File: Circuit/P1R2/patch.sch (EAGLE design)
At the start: 34 parts, among them U1 MK20DX256VLH7, U2 TPS61200, Y1 32.768KHz, Y2 16Mhz/8pF

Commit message: Forum boards done
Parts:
- removed JP1: (no value), SparkFun-Connectors:M07
- removed LED: AMBER/ 592 nm, appfruits:LED-AMBER
- removed R30: 470, appfruits:RESISTOR-470
- added C10: 4.7 pF, SparkFun-Capacitors:CAP0603-CAP
- added C12: 1.0 pF, SparkFun-Capacitors:CAP0603-CAP
- added C13: 1.5 pF, SparkFun-Capacitors:CAP0603-CAP
- added C14, C15: 22 pF, SparkFun-Capacitors:CAP0603-CAP
- added C22: 1 uF, SparkFun-Capacitors:CAP0603-CAP
- added C23, C7: 15 pF, SparkFun-Capacitors:CAP0603-CAP
- added C24, C25: .1 uF, SparkFun-Capacitors:CAP0603-CAP
- added C6: 5.6 pF, SparkFun-Capacitors:CAP0603-CAP
- added C8: 33 nF, SparkFun-Capacitors:CAP0603-CAP
- added C9: 2.2 nF, SparkFun-Capacitors:CAP0603-CAP
- added JP5: (no value), SparkFun-Connectors:M02PTH
- added JP6: M100.1, umich:M100.1
- added L2: 2.7 nH, SparkFun-Passives:INDUCTOR0402
- added L5: 8.2 nH, SparkFun-Passives:INDUCTOR0402
- added L6: 3.9 nH, SparkFun-Passives:INDUCTOR0402
- added MESH: NRF24L01, RF:NRF24L01
- added R1, R5, R8: 12k, SparkFun-Resistors:RESISTOR0603-RES
- added R11: 1M, SparkFun-Resistors:RESISTOR0603-RES
- added R12: 22k, SparkFun-Resistors:RESISTOR0603-RES
- added R13, R14, R15: 10k, SparkFun-Resistors:RESISTOR0603-RES
- added S1: (no value), SparkFun-Electromechanical:SWITCH-SPDT-SMD-A
- added U$1, U$2: ANTENNA2SMD, SparkFun-RF:ANTENNA2SMD
- added U$3: 25Q40, wifi:25Q40
- added U3: MPU-9250, chips:MPU-9250
- added WIFI: ESP8266EX, wifi:ESP8266EX
- added Y3, Y4: 16 Mhz, SparkFun-FreqCtrl:CRYSTAL5X3
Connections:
- net 18/SDA renamed PTB3
- net 19/SCL renamed PTB2
- removed net 16: JP2.3, U1.PTB0
- removed net 17: JP2.4, U1.PTB1
- removed net 20: JP2.5
- removed net 28: LED.A, U1.PTC8
- removed net PGND: C1.2, C3.2, C4.2, U2.GND, U2.PAD@1, U2.PAD@2, U2.PAD@3, U2.PAD@4, U2.PAD@5, U2.PGND
- new net 3.3V1: C22.2, C24.2, C25.1, MESH.VDD/15, MESH.VDD/18, MESH.VDD/7, R8.2, U$3.VCC, U3.VDD, U3.VDDIO, WIFI.CHIP_EN/7, WIFI.VDD3P3/3, WIFI.VDD3P3/4, WIFI.VDDA/1, WIFI.VDDD/29, WIFI.VDDPST/11, WIFI.VDDPST/17
- new net CE: MESH.CE/1
- new net CSN: MESH.CSN/2
- new net GND1: C10.2, C12.2, C14.2, C15.2, C22.1, C23.2, C24.1, C25.2, C7.2, C8.1, C9.2, MESH.VSS/14, MESH.VSS/17, MESH.VSS/20, MESH.VSS/8, R12.2, R5.1, U$3.GND, WIFI.GND/33
- new net IQR: MESH.IRQ/6
- new net MISO: MESH.MISO/5
- new net MOSI: MESH.MOSI/4
- new net N$13: C6.2, WIFI.LNA/2
- new net N$16: C6.1, U$1.SIGNAL
- new net N$17: C14.1, MESH.XC2/9, R11.1, Y4.1
- new net N$19: C10.1, C9.1, L2.2, MESH.VDD_PA/11
- new net N$20: L5.1, L6.1, MESH.ANT2/13
- new net N$21: C8.2, MESH.DVDD/19
- new net N$22: MESH.GND
- new net N$23: L2.1, L5.2, MESH.ANT1/12
- new net N$24: MESH.IREF/16, R12.1
- new net N$25: C13.1, L6.2
- new net N$26: C12.1, C13.2, U$2.SIGNAL
- new net N$31: R8.1, WIFI.GPIO2/14
- new net N$32: R5.2, WIFI.MTCK/12
- new net N$33: U3.FSYNC
- new net N$34: U3.REGOUT
- new net N$35: U3.AUX_DA
- new net N$36: U3.AUX_CL
- new net N$37: U3.GND
- new net N$38: WIFI.RES12K/31
- new net N$39: U3.INT
- new net N$40: U3.!CS
- new net PTB0: U1.PTB0
- new net PTB1: U1.PTB1
- new net RST: R1.1, WIFI.EXT_RSTB/32
- new net RTC: WIFI.VDD_RTC/5
- new net RX_W: WIFI.U0TXD/26
- new net SCK: MESH.SCK/3
- new net SCL: R14.2
- new net SD-CLK: U$3.CLK, WIFI.SD_CLK/21
- new net SD-CMD: U$3.CS#, WIFI.SD_CMD/20
- new net SD-D0: U$3.DO, WIFI.SD_DATA_0/22
- new net SD-D1: U$3.DIO, WIFI.SD_DATA_1/23
- new net SD-D2: U$3.HOLD#, WIFI.SD_DATA_2/18
- new net SD-D3: U$3.WP#, WIFI.SD_DATA_3/19
- new net SDA: R13.2
- new net SDO: R15.2
- new net TOUT: WIFI.TOUT/6
- new net TX_W: WIFI.U0RXD/25
- new net VDD: R13.1, R14.1, R15.1, WIFI.VDDA/30
- new net VRAW: JP5.2, S1.P
- new net XTAL_IN: C23.1, WIFI.XTAL_IN/28, Y3.2
- new net XTAL_OUT: C7.1, WIFI.XTAL_OUT/27, Y3.1
- net 14: no longer JP2.1
- net 15: no longer JP2.2
- net 21: no longer JP2.6
- net 22: no longer JP2.7
- net 23: no longer JP2.8
- net 3.3V: now also JP6.1, LED1.A; no longer LED1.C
- net GND: now also C1.2, C3.2, C4.2, JP5.1, JP6.10, U2.GND, U2.PAD@1, U2.PAD@2, U2.PAD@3, U2.PAD@4, U2.PAD@5, U2.PGND; no longer R30.1
- net ID: now also JP6.6; no longer JP1.5
- net N$1: now also LED1.C; no longer LED1.A
- net N$18: now also C15.1, MESH.XC1/10, R11.2, Y4.2; no longer LED.C, R30.2
- net PTA2: now also JP6.3; no longer JP1.2
- net RESET_B: now also JP6.2; no longer JP1.1
- net SWD_CLK: now also JP6.4; no longer JP1.3
- net SWD_DIO: now also JP6.5; no longer JP1.4
- net USB_D_N: now also JP6.8; no longer JP1.7
- net USB_D_P: now also JP6.7; no longer JP1.6
- net VCC: now also JP6.9, S1.O

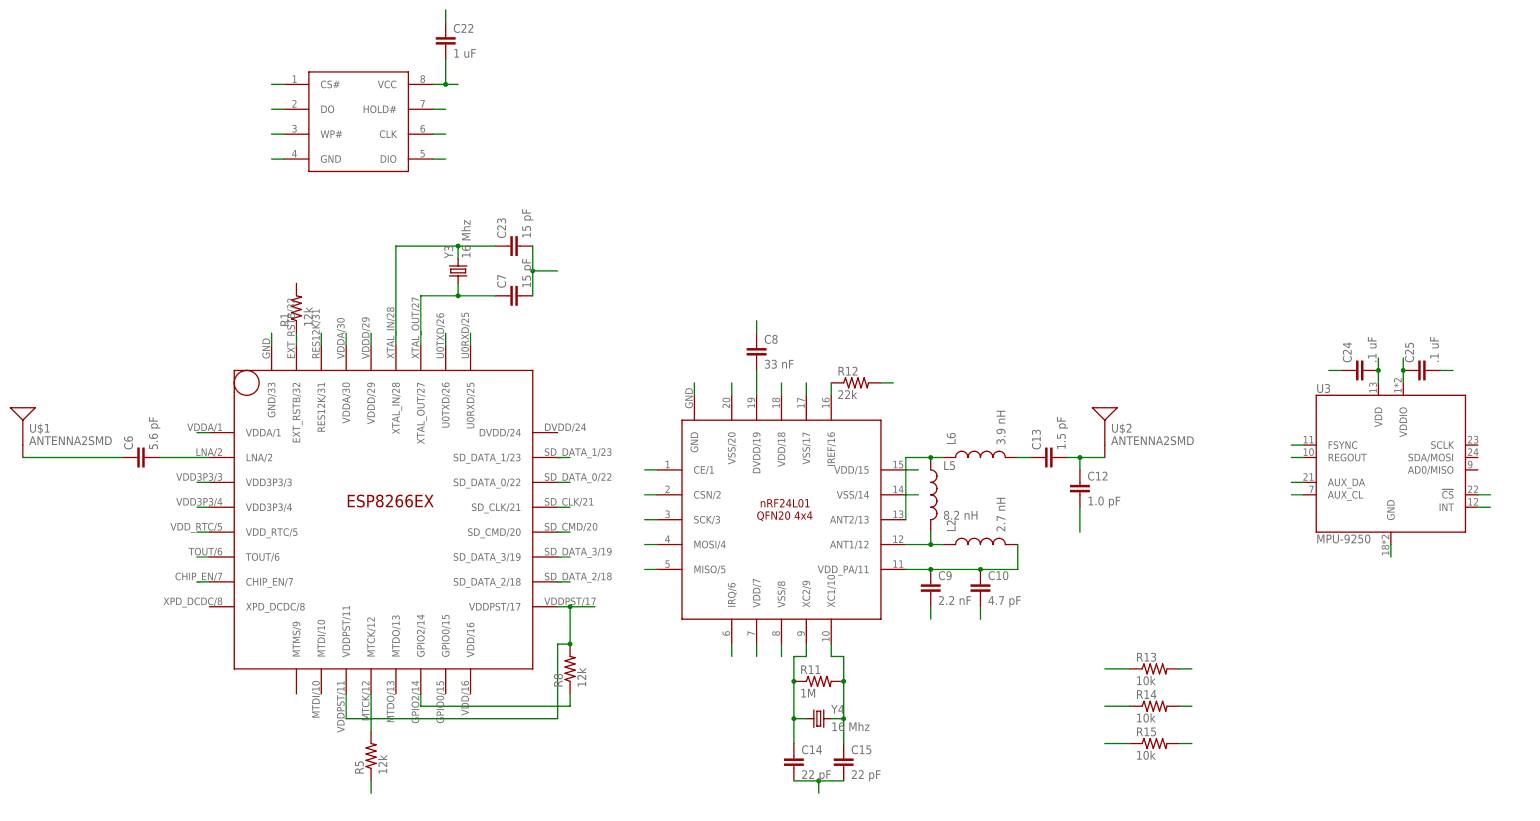
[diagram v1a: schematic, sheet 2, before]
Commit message: Mesh and IMU in place
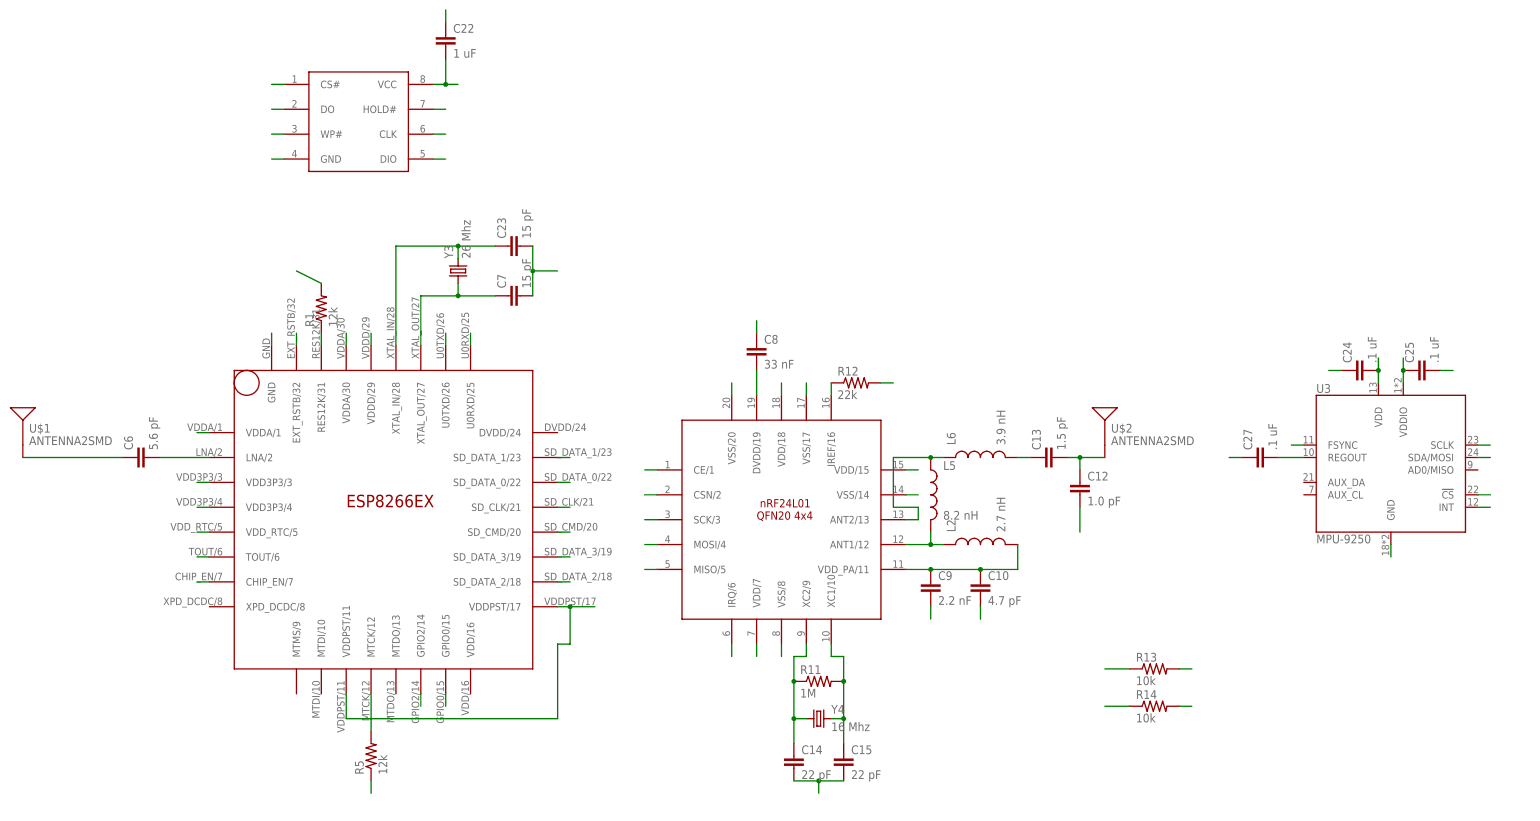
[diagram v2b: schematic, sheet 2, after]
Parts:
- removed R15: 10k, SparkFun-Resistors:RESISTOR0603-RES
- removed R8: 12k, SparkFun-Resistors:RESISTOR0603-RES
- added C27: .1 uF, SparkFun-Capacitors:CAP0603-CAP
- Y3: value 16 Mhz -> 26 Mhz
- renumbered MESH to U$4, WIFI to U$6
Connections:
- net 14 renamed PTD1
- net 2 renamed PTD0
- net 21 renamed PTD6
- net 23 renamed PTC2
- net 24 renamed PTA5
- net 26 renamed PTE1
- net 29 renamed PTC10
- net 3 renamed PTA12
- net 30 renamed PTC11
- net 31 renamed PTE0
- net 33 renamed PTA4
- net 4 renamed PTA13
- net 5 renamed PTD7
- net 6 renamed PTD4
- net 7 renamed PTD2
- net 8 renamed PTD3
- net 9 renamed PTC3
- net N$7 renamed PTD5
- removed net 0: U1.PTB16
- removed net 1: U1.PTB17
- removed net 10: U1.PTC4
- removed net 11/MOSI: U1.PTC6
- removed net 12/MISO: U1.PTC7
- removed net 13/SCK: U1.PTC5
- removed net 15: U1.PTC0
- removed net 22: U1.PTC1
- removed net 25: U1.PTB19
- removed net 27: U1.PTC9
- removed net 3.3V1: C22.2, C24.2, C25.1, R8.2, U$3.VCC, U$4.VDD/15, U$4.VDD/18, U$4.VDD/7, U$6.CHIP_EN/7, U$6.VDD3P3/3, U$6.VDD3P3/4, U$6.VDDA/1, U$6.VDDD/29, U$6.VDDPST/11, U$6.VDDPST/17, U3.VDD, U3.VDDIO
- removed net 32: U1.PTB18
- removed net CE: U$4.CE/1
- removed net CSN: U$4.CSN/2
- removed net GND1: C10.2, C12.2, C14.2, C15.2, C22.1, C23.2, C24.1, C25.2, C7.2, C8.1, C9.2, R12.2, R5.1, U$3.GND, U$4.VSS/14, U$4.VSS/17, U$4.VSS/20, U$4.VSS/8, U$6.GND/33
- removed net IQR: U$4.IRQ/6
- removed net MISO: U$4.MISO/5
- removed net MOSI: U$4.MOSI/4
- removed net N$22: U$4.GND
- removed net N$31: R8.1, U$6.GPIO2/14
- removed net N$33: U3.FSYNC
- removed net N$35: U3.AUX_DA
- removed net N$36: U3.AUX_CL
- removed net N$37: U3.GND
- removed net N$39: U3.INT
- removed net N$40: U3.!CS
- removed net RST: R1.1, U$6.EXT_RSTB/32
- removed net RX_W: U$6.U0TXD/26
- removed net SCK: U$4.SCK/3
- removed net SDO: R15.2
- removed net TX_W: U$6.U0RXD/25
- new net PTB16: U$6.U0RXD/25, U1.PTB16
- new net PTB17: U$6.U0TXD/26, U1.PTB17
- new net PTB18: U$6.GPIO0/15, U1.PTB18
- new net PTB19: U$6.GPIO2/14, U1.PTB19
- new net PTC0: U$6.EXT_RSTB/32, U1.PTC0
- new net PTC1: U$6.CHIP_EN/7, U1.PTC1
- new net PTC4: U$4.CSN/2, U1.PTC4
- new net PTC5: U$4.SCK/3, U1.PTC5
- new net PTC6: U$4.MOSI/4, U1.PTC6
- new net PTC7: U$4.MISO/5, U1.PTC7
- new net PTC8: U$4.IRQ/6, U1.PTC8
- new net PTC9: U$4.CE/1, U1.PTC9
- net 3.3V: now also C22.2, C24.2, C25.1, R13.1, R14.1, U$3.VCC, U$4.VDD/18, U$4.VDD/7, U$6.VDD3P3/3, U$6.VDD3P3/4, U$6.VDDA/1, U$6.VDDD/29, U$6.VDDPST/11, U$6.VDDPST/17, U3.!CS, U3.VDD, U3.VDDIO
- net GND: now also C10.2, C12.2, C14.2, C15.2, C22.1, C23.2, C24.1, C25.2, C27.1, C7.2, C8.1, C9.2, R1.2, R12.2, R5.1, U$3.GND, U$4.VSS/17, U$4.VSS/20, U$4.VSS/8, U$6.GND, U3.GND
- net N$34: now also C27.2
- net N$38: now also R1.1
- net PTB0: now also U3.INT
- net PTB1: now also U3.FSYNC
- net SCL: now also U3.SCLK
- net SDA: now also U3.SDA/MOSI
- net VDD: no longer R13.1, R14.1, R15.1
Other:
- moved on the sheet: R1

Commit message: GPIO wired yo
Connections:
- net PTC10: now also JP2.8
- net PTC11: now also JP2.7
- net PTD0: now also JP2.6
- net PTD1: now also JP2.5
- net PTD2: now also JP2.4
- net PTD3: now also JP2.3
- net PTD4: now also JP2.2
- net PTD5: now also JP2.1
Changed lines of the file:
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@@
 <wire x1="203.2" y1="-58.42" x2="210.82" y2="-58.42" width="0.1524" layer="91"/>
+</segment>
+<segment>
+<pinref part="JP2" gate="G$1" pin="1"/>
+<wire x1="246.38" y1="-53.34" x2="241.3" y2="-53.34" width="0.1524" layer="91"/>
 </segment>
 </net>
@@
 <wire x1="203.2" y1="-73.66" x2="210.82" y2="-73.66" width="0.1524" layer="91"/>
 </segment>
+<segment>
+<pinref part="JP2" gate="G$1" pin="5"/>
+<wire x1="246.38" y1="-63.5" x2="241.3" y2="-63.5" width="0.1524" layer="91"/>
+</segment>
 </net>
 <net name="PTC4" class="0">
@@
 <wire x1="203.2" y1="-93.98" x2="210.82" y2="-93.98" width="0.1524" layer="91"/>
 </segment>
+<segment>
+<pinref part="JP2" gate="G$1" pin="3"/>
+<wire x1="246.38" y1="-58.42" x2="241.3" y2="-58.42" width="0.1524" layer="91"/>
+</segment>
 </net>
 <net name="PTD2" class="0">
@@
 <wire x1="203.2" y1="-96.52" x2="210.82" y2="-96.52" width="0.1524" layer="91"/>
 </segment>
+<segment>
+<pinref part="JP2" gate="G$1" pin="4"/>
+<wire x1="246.38" y1="-60.96" x2="241.3" y2="-60.96" width="0.1524" layer="91"/>
+</segment>
 </net>
 <net name="PTD4" class="0">
@@
 <pinref part="U1" gate="G$1" pin="PTD4"/>
 <wire x1="203.2" y1="-99.06" x2="210.82" y2="-99.06" width="0.1524" layer="91"/>
+</segment>
+<segment>
+<pinref part="JP2" gate="G$1" pin="2"/>
+<wire x1="246.38" y1="-55.88" x2="241.3" y2="-55.88" width="0.1524" layer="91"/>
 </segment>
 </net>
@@
 <pinref part="U1" gate="G$1" pin="PTD0"/>
 <wire x1="203.2" y1="-109.22" x2="210.82" y2="-109.22" width="0.1524" layer="91"/>
+</segment>
+<segment>
+<pinref part="JP2" gate="G$1" pin="6"/>
+<wire x1="246.38" y1="-66.04" x2="241.3" y2="-66.04" width="0.1524" layer="91"/>
 </segment>
 </net>
@@
 <wire x1="203.2" y1="-134.62" x2="210.82" y2="-134.62" width="0.1524" layer="91"/>
 </segment>
+<segment>
+<pinref part="JP2" gate="G$1" pin="7"/>
+<wire x1="246.38" y1="-68.58" x2="241.3" y2="-68.58" width="0.1524" layer="91"/>
+</segment>
 </net>
 <net name="PTC10" class="0">
@@
 <wire x1="203.2" y1="-137.16" x2="210.82" y2="-137.16" width="0.1524" layer="91"/>
 </segment>
+<segment>
+<pinref part="JP2" gate="G$1" pin="8"/>
+<wire x1="246.38" y1="-71.12" x2="241.3" y2="-71.12" width="0.1524" layer="91"/>
+</segment>
 </net>

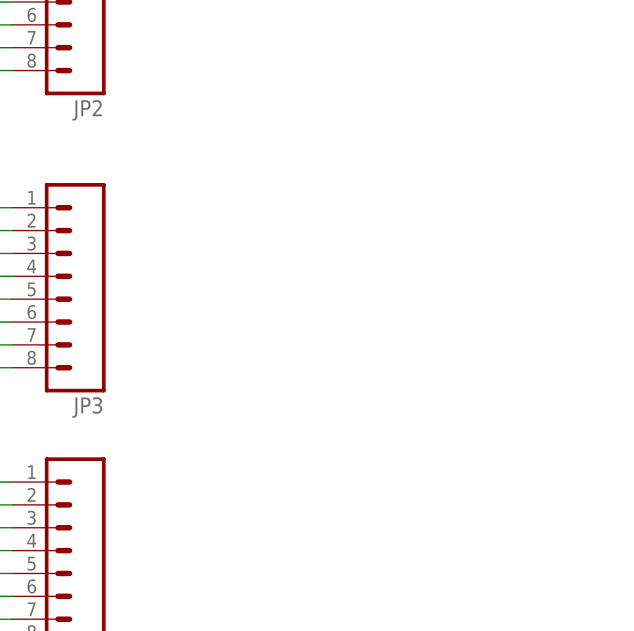
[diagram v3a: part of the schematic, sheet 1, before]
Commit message: LEDs and GPIO finished. Rough R2 board done
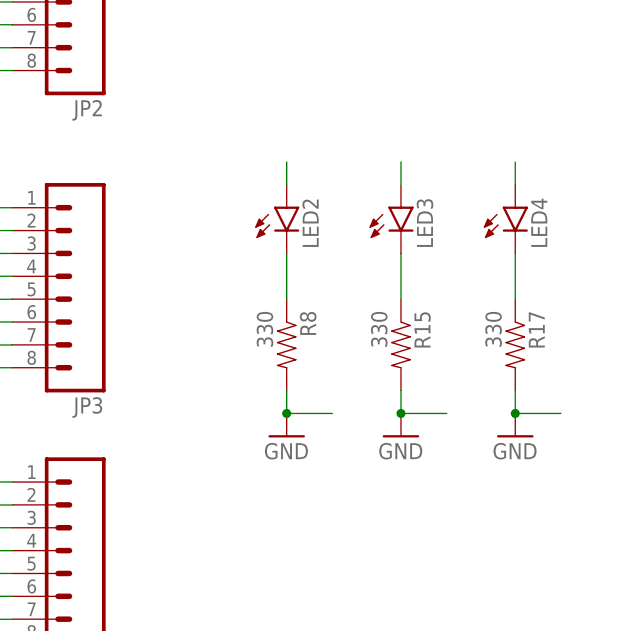
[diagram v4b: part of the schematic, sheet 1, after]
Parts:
- added LED2, LED3, LED4: (no value), appfruits:LED-GREEN
- added R15, R17, R8: 330, appfruits:RESISTOR-470
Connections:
- new net N$7: LED2.C, R8.1
- new net N$8: LED3.C, R15.1
- new net N$9: LED4.C, R17.1
- net GND: now also R15.2, R17.2, R8.2
- net PTB2: now also LED2.A
- net PTC2: now also LED3.A
- net PTC3: now also LED4.A
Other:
- note added: "GND"
- note added: "I2C power"
- note added: "SCL"
- note added: "SDA"
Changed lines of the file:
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@@
 <part name="U$4" library="RF" deviceset="NRF24L01" device=""/>
 <part name="U$6" library="wifi" deviceset="ESP8266EX" device=""/>
+<part name="R8" library="appfruits" deviceset="RESISTOR" device="-470" value="330"/>
+<part name="LED2" library="appfruits" deviceset="LED" device="-GREEN"/>
+<part name="GND2" library="supply1" deviceset="GND" device=""/>
+<part name="R15" library="appfruits" deviceset="RESISTOR" device="-470" value="330"/>
+<part name="LED3" library="appfruits" deviceset="LED" device="-GREEN"/>
+<part name="GND3" library="supply1" deviceset="GND" device=""/>
+<part name="R17" library="appfruits" deviceset="RESISTOR" device="-470" value="330"/>
+<part name="LED4" library="appfruits" deviceset="LED" device="-GREEN"/>
+<part name="GND6" library="supply1" deviceset="GND" device=""/>
 </parts>
 <sheets>
@@
 <instance part="JP6" gate="G$1" x="55.88" y="-142.24"/>
 <instance part="S1" gate="1" x="33.02" y="-15.24"/>
+<instance part="R8" gate="G$1" x="276.86" y="-101.6" rot="R270"/>
+<instance part="LED2" gate="G$1" x="276.86" y="-86.36"/>
+<instance part="GND2" gate="1" x="276.86" y="-111.76"/>
+<instance part="R15" gate="G$1" x="289.56" y="-101.6" rot="R270"/>
+<instance part="LED3" gate="G$1" x="289.56" y="-86.36"/>
+<instance part="GND3" gate="1" x="289.56" y="-111.76"/>
+<instance part="R17" gate="G$1" x="302.26" y="-101.6" rot="R270"/>
+<instance part="LED4" gate="G$1" x="302.26" y="-86.36"/>
+<instance part="GND6" gate="1" x="302.26" y="-111.76"/>
 </instances>
 <busses>
@@
 <pinref part="JP5" gate="G$1" pin="1"/>
 <wire x1="25.4" y1="-17.78" x2="27.94" y2="-17.78" width="0.1524" layer="91"/>
+</segment>
+<segment>
+<pinref part="R8" gate="G$1" pin="2"/>
+<pinref part="GND2" gate="1" pin="GND"/>
+<wire x1="276.86" y1="-106.68" x2="276.86" y2="-109.22" width="0.1524" layer="91"/>
+<junction x="276.86" y="-109.22"/>
+<wire x1="276.86" y1="-109.22" x2="281.94" y2="-109.22" width="0.1524" layer="91"/>
+</segment>
+<segment>
+<pinref part="R15" gate="G$1" pin="2"/>
+<pinref part="GND3" gate="1" pin="GND"/>
+<wire x1="289.56" y1="-106.68" x2="289.56" y2="-109.22" width="0.1524" layer="91"/>
+<junction x="289.56" y="-109.22"/>
+<wire x1="289.56" y1="-109.22" x2="294.64" y2="-109.22" width="0.1524" layer="91"/>
+</segment>
+<segment>
+<pinref part="R17" gate="G$1" pin="2"/>
+<pinref part="GND6" gate="1" pin="GND"/>
+<wire x1="302.26" y1="-106.68" x2="302.26" y2="-109.22" width="0.1524" layer="91"/>
+<junction x="302.26" y="-109.22"/>
+<wire x1="302.26" y1="-109.22" x2="307.34" y2="-109.22" width="0.1524" layer="91"/>
 </segment>
 </net>
@@
 <wire x1="203.2" y1="-60.96" x2="210.82" y2="-60.96" width="0.1524" layer="91"/>
 </segment>
+<segment>
+<pinref part="LED2" gate="G$1" pin="A"/>
+<wire x1="276.86" y1="-83.82" x2="276.86" y2="-81.28" width="0.1524" layer="91"/>
+</segment>
 </net>
 <net name="USB_D_P" class="1">
@@
 <wire x1="203.2" y1="-50.8" x2="210.82" y2="-50.8" width="0.1524" layer="91"/>
 </segment>
+<segment>
+<pinref part="LED3" gate="G$1" pin="A"/>
+<wire x1="289.56" y1="-83.82" x2="289.56" y2="-81.28" width="0.1524" layer="91"/>
+</segment>
 </net>
 <net name="PTC1" class="0">
@@
 <pinref part="U1" gate="G$1" pin="PTC3"/>
 <wire x1="203.2" y1="-91.44" x2="210.82" y2="-91.44" width="0.1524" layer="91"/>
+</segment>
+<segment>
+<pinref part="LED4" gate="G$1" pin="A"/>
+<wire x1="302.26" y1="-83.82" x2="302.26" y2="-81.28" width="0.1524" layer="91"/>
 </segment>
 </net>
@@
 <pinref part="U1" gate="G$1" pin="PTC8"/>
 <wire x1="203.2" y1="-139.7" x2="210.82" y2="-139.7" width="0.1524" layer="91"/>
+</segment>
+</net>
+<net name="N$7" class="0">
+<segment>
+<pinref part="R8" gate="G$1" pin="1"/>
+<pinref part="LED2" gate="G$1" pin="C"/>
+<wire x1="276.86" y1="-91.44" x2="276.86" y2="-96.52" width="0.1524" layer="91"/>
+</segment>
+</net>
+<net name="N$8" class="0">
+<segment>
+<pinref part="R15" gate="G$1" pin="1"/>
+<pinref part="LED3" gate="G$1" pin="C"/>
+<wire x1="289.56" y1="-91.44" x2="289.56" y2="-96.52" width="0.1524" layer="91"/>
+</segment>
+</net>
+<net name="N$9" class="0">
+<segment>
+<pinref part="R17" gate="G$1" pin="1"/>
+<pinref part="LED4" gate="G$1" pin="C"/>
+<wire x1="302.26" y1="-91.44" x2="302.26" y2="-96.52" width="0.1524" layer="91"/>
 </segment>
 </net>
@@
 <sheet>
 <plain>
+<text x="190.5" y="17.78" size="1.778" layer="91">I2C power</text>
+<text x="215.9" y="22.86" size="1.778" layer="91">SCL</text>
+<text x="215.9" y="15.24" size="1.778" layer="91">SDA</text>
+<text x="276.86" y="66.04" size="1.778" layer="91">SDA</text>
+<text x="276.86" y="68.58" size="1.778" layer="91">SCL</text>
+<text x="33.02" y="104.14" size="1.778" layer="91">GND</text>
+<text x="20.32" y="91.44" size="1.778" layer="91">GND</text>
+<text x="43.18" y="-5.08" size="1.778" layer="91">GND</text>
+<text x="119.38" y="96.52" size="1.778" layer="91">GND</text>
+<text x="134.62" y="83.82" size="1.778" layer="91">GND</text>
+<text x="251.46" y="43.18" size="1.778" layer="91">GND</text>
 </plain>
 <instances>
